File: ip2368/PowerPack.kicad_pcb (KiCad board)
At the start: 2 copper layers, 79 x 31 mm, 75 parts, among them CN1 XT30PW-M, Q1 WSD3066DN33, U1 IP2368_BZ_VGLIP_C5203723, U2 ME6203A50PG

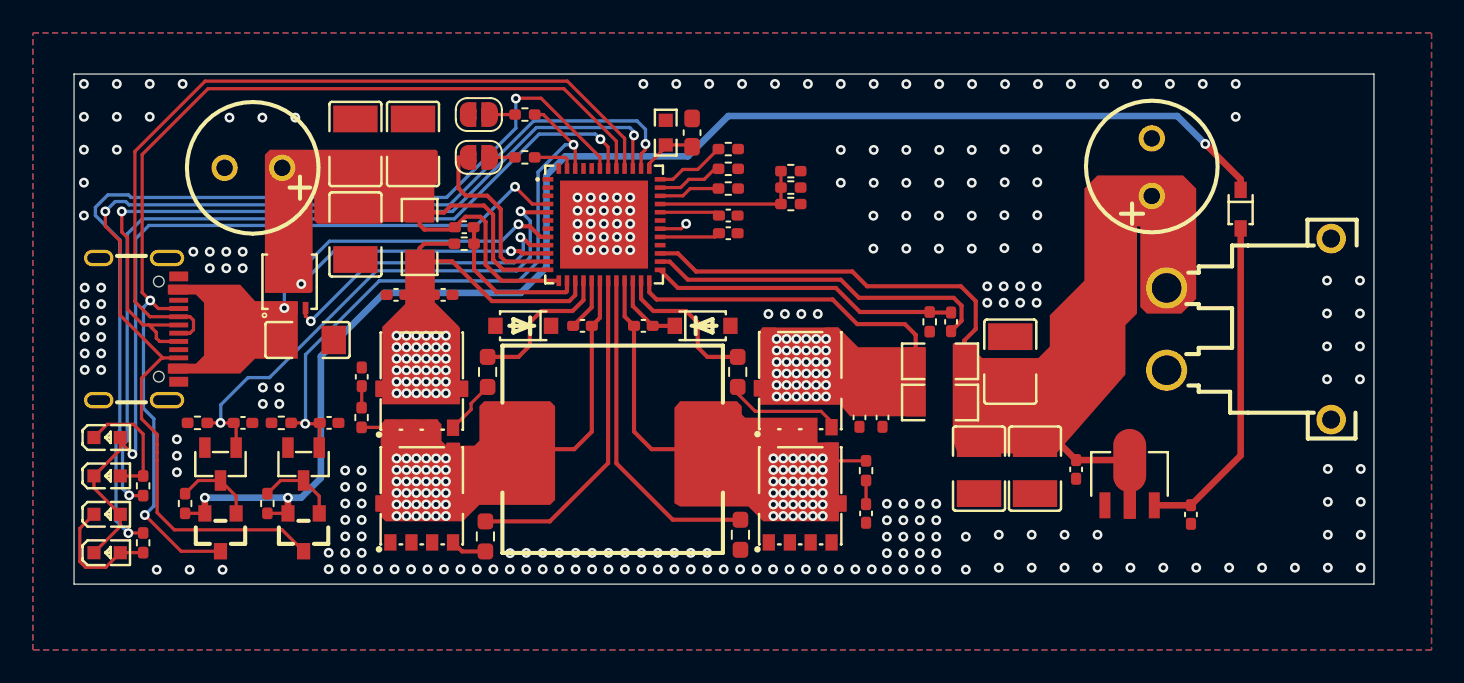
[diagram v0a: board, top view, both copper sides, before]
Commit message: start new board design based on the ip2366
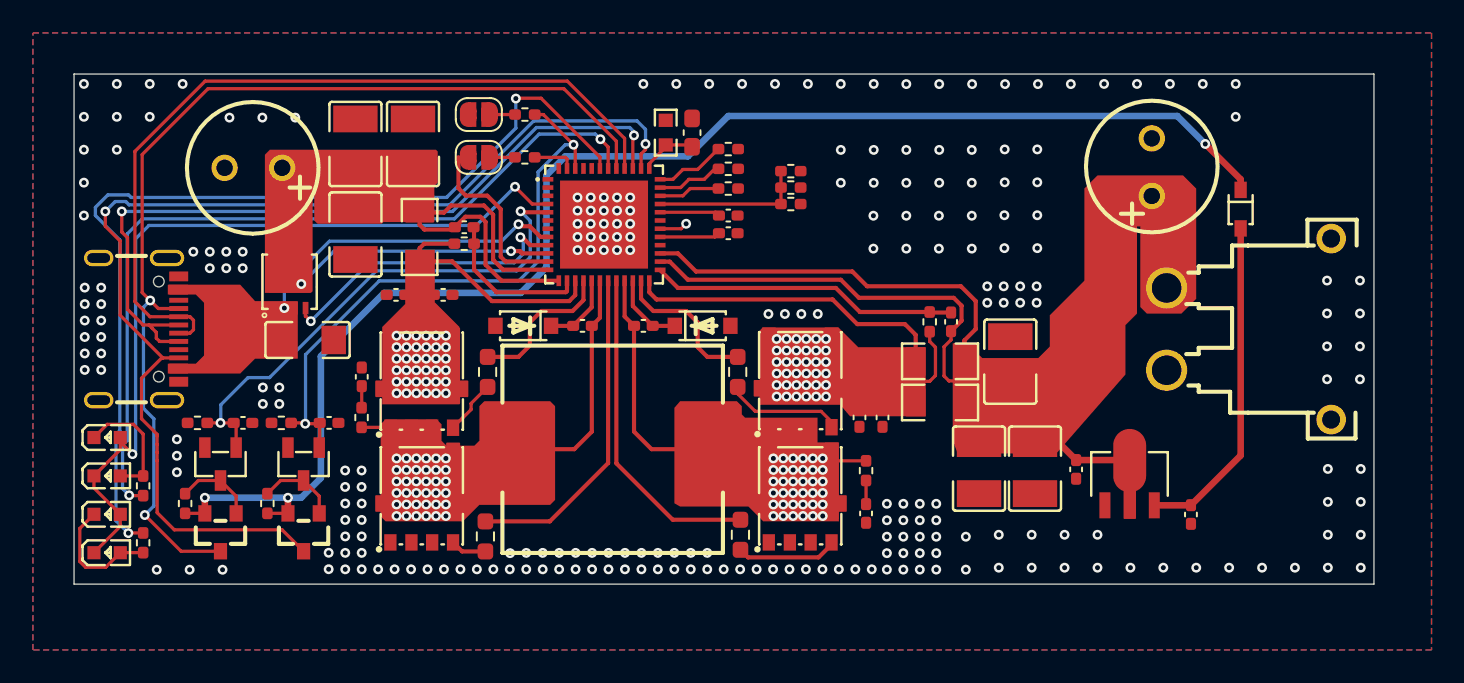
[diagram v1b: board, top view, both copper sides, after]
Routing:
- net Net-(QRT1-D): track 19.6 -> 27.6 mm
- net VBUSR_Source: track 51.8 -> 59.1 mm
- net Net-(QRB1-G): track 0.00 -> 6.18 mm
- net Net-(D1-K): track 3.21 -> 4.56 mm
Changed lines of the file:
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@@
 	(gr_poly
 		(pts
-			(xy 105.7 92.8) (xy 105.7 92.8) (xy 110.1 92.8) (xy 111 93.8) (xy 113.6 93.8) (xy 113.6 97.3) (xy 111 97.3)
-			(xy 110.1 98.2) (xy 105.7 98.2) (xy 105.7 97.6) (xy 107.4 97.6) (xy 107.9 97.1) (xy 107.9 93.9) (xy 107.4 93.4)
-			(xy 105.7 93.4)
+			(xy 105.7 92.8) (xy 110.1 92.8) (xy 111 93.8) (xy 113.6 93.8) (xy 113.6 97.3) (xy 111 97.3) (xy 110.1 98.2)
+			(xy 105.7 98.2) (xy 105.7 97.6) (xy 107.4 97.6) (xy 107.9 97.1) (xy 107.9 93.9) (xy 107.4 93.4) (xy 105.7 93.4)
 		)
 		(stroke
@@
 	)
 	(segment
+		(start 153.3 96.15)
+		(end 152.875 96.575)
+		(width 0.2)
+		(layer "F.Cu")
+		(net 1)
+	)
+	(segment
+		(start 153.3 95.6275)
+		(end 153.3 96.15)
+		(width 0.2)
+		(layer "F.Cu")
+		(net 1)
+	)
+	(segment
 		(start 153.938 94.07564)
 		(end 153.938 94.9895)
@@
 	)
 	(segment
+		(start 152.875 96.575)
+		(end 152.875 98.35)
+		(width 0.2)
+		(layer "F.Cu")
+		(net 1)
+	)
+	(segment
 		(start 154.11 96.19)
 		(end 154.8 95.5)
@@
 	)
 	(segment
+		(start 153.175 98.65)
+		(end 156.823 98.65)
+		(width 0.2)
+		(layer "F.Cu")
+		(net 1)
+	)
+	(segment
 		(start 135.62 91.4)
 		(end 136.2 91.4)
@@
 	)
 	(segment
+		(start 152.875 98.35)
+		(end 153.175 98.65)
+		(width 0.2)
+		(layer "F.Cu")
+		(net 1)
+	)
+	(segment
 		(start 147.3 92)
 		(end 137.8 92)
@@
 	)
 	(segment
+		(start 156.9 98.727)
+		(end 156.9 99)
+		(width 0.2)
+		(layer "F.Cu")
+		(net 1)
+	)
+	(segment
+		(start 156.823 98.65)
+		(end 156.9 98.727)
+		(width 0.2)
+		(layer "F.Cu")
+		(net 1)
+	)
+	(segment
 		(start 136.7 90.9)
 		(end 135.62 90.9)
@@
 	)
 	(segment
+		(start 128.994 95.304)
+		(end 128.99 95.3)
+		(width 0.254)
+		(layer "F.Cu")
+		(net 5)
+	)
+	(segment
 		(start 131.46 94.1765)
 		(end 130.3325 95.304)
@@
 	)
 	(segment
+		(start 130.3325 95.304)
+		(end 128.994 95.304)
+		(width 0.254)
+		(layer "F.Cu")
+		(net 5)
+	)
+	(segment
 		(start 133.96 92.56)
 		(end 133.96 94.0965)
@@
 	)
 	(segment
+		(start 152 98.675)
+		(end 147.285 98.675)
+		(width 0.2)
+		(layer "F.Cu")
+		(net 54)
+	)
+	(segment
+		(start 152.35 96.6)
+		(end 152.35 98.325)
+		(width 0.2)
+		(layer "F.Cu")
+		(net 54)
+	)
+	(segment
+		(start 152.35 98.325)
+		(end 152 98.675)
+		(width 0.2)
+		(layer "F.Cu")
+		(net 54)
+	)
+	(segment
+		(start 152 95.6575)
+		(end 152 96.25)
+		(width 0.2)
+		(layer "F.Cu")
+		(net 54)
+	)
+	(segment
 		(start 135.4 93.7)
 		(end 146.1 93.7)
@@
 		(net 54)
 	)
+	(segment
+		(start 152 96.25)
+		(end 152.35 96.6)
+		(width 0.2)
+		(layer "F.Cu")
+		(net 54)
+	)
 	(via
 		(at 144.5 98.2)
@@
 	)
 	(segment
+		(start 140.5 108.9125)
+		(end 140.9625 109.375)
+		(width 0.254)
+		(layer "F.Cu")
+		(net 57)
+	)
+	(segment
+		(start 146.034 108.589)
+		(end 146.034 108.464)
+		(width 0.254)
+		(layer "F.Cu")
+		(net 57)
+	)
+	(segment
+		(start 145.248 109.375)
+		(end 146.034 108.589)
+		(width 0.254)
+		(layer "F.Cu")
+		(net 57)
+	)
+	(segment
+		(start 140.9625 109.375)
+		(end 145.248 109.375)
+		(width 0.254)
+		(layer "F.Cu")
+		(net 57)
+	)
+	(segment

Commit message: add teardrops
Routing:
- net Net-(QLB1-D): track 19.5 -> 16.0 mm
- net Net-(QRB1-G): track 6.18 -> 6.72 mm
- net GND: vias 239 -> 241
